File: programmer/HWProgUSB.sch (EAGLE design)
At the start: 98 parts, among them X2 P_AVR_P

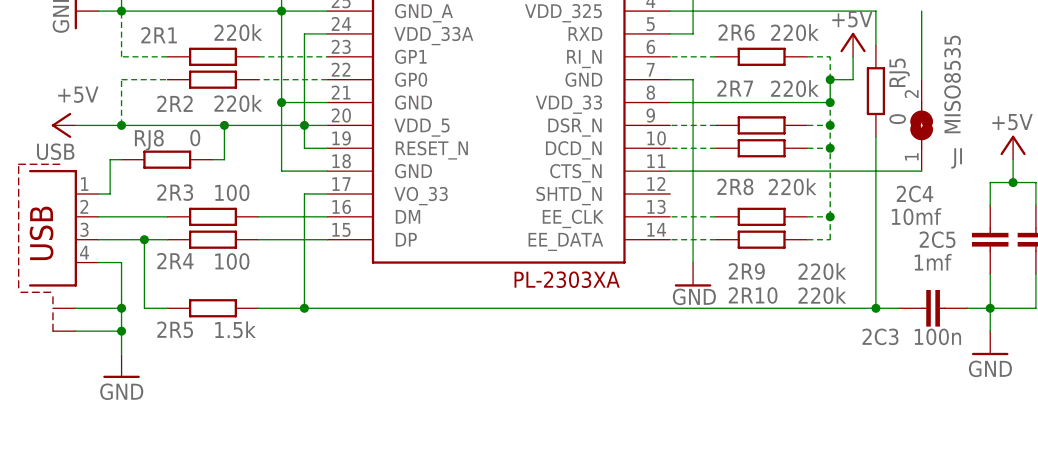
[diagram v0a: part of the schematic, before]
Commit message: add 3v3 led ..
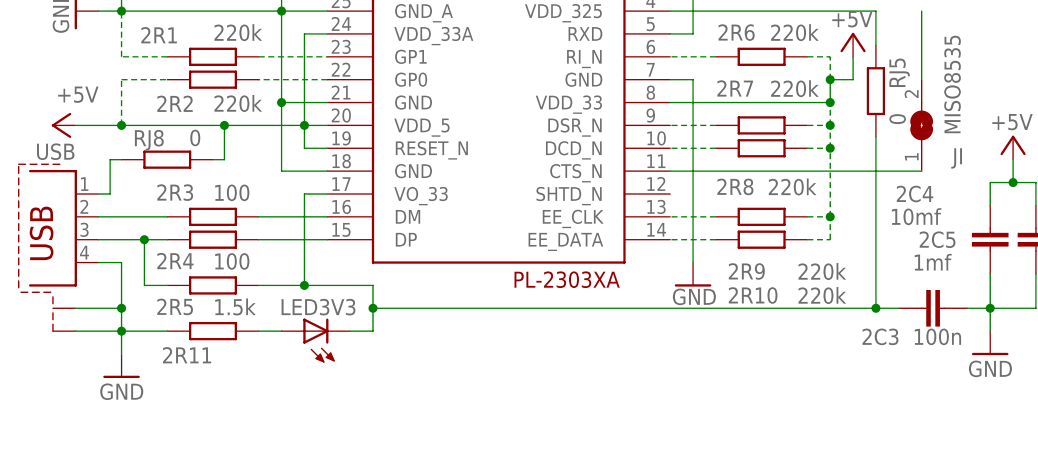
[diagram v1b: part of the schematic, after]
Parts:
- added 2R11: (no value), resistor:R-EU_R0603
- added LED3V3: (no value), led:LEDCHIPLED_0603
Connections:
- new net N$22: 2R11.1, LED3V3.A
- net 3VUSB: now also LED3V3.C
- net GND: now also 2R11.2
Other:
- moved on the sheet: 2R5
